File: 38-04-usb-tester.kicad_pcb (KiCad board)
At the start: 2 copper layers, 131.7 x 103.7 mm, 63 parts, among them J1 Conn_1x05, J2 USB_C_12401832E402A, J3 USB_C_12401832E402A, J4 USB_Micro-B_KH-MICRO5P-JN, J5 USB_Mini-B_U-M-M5DD-W-1, J6 USB3_A_HC-USB3.0-L168-WP, SW1 SW_SPDT, SW2 ZX-1.27BM-4PSMD, U1 STM32C031K6Tx

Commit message: pre commit to importing template
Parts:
- R1, R2, R3, R5: footprint Resistor_SMD:R_0201_0603Metric -> Resistor_SMD:R_0805_2012Metric_Pad1.20x1.40mm_HandSolder
- moved J1 54.7 mm to (183.9, 107.4), turned to 0 degrees
- moved C2 53.6 mm to (174.5, 123.2), turned to 0 degrees
- moved C1 40.9 mm to (131.2, 120.0), turned to -90 degrees
- moved C5 38.6 mm to (167.4, 120.4)
- moved SW2 36.6 mm to (172.3, 133.6)
- moved R5 29.8 mm to (171.2, 120.4)
- moved BT1 21.0 mm to (154.9, 114.2), turned to -90 degrees
- moved RN1 11.0 mm to (175.8, 101.3)
- moved RN2 11.0 mm to (175.8, 97.0)
- moved RN4 11.0 mm to (175.8, 87.6)
- moved RN5 11.0 mm to (175.8, 93.0)
- moved H10 10.1 mm to (118.5, 80.5)
- moved H2 9.78 mm to (191.3, 140.0)
- moved H5 8.98 mm to (118.5, 140.0)
- moved H7 8.18 mm to (196.9, 86.9)
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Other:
- board size 131.7 x 103.7 mm -> 125.9 x 97.8 mm

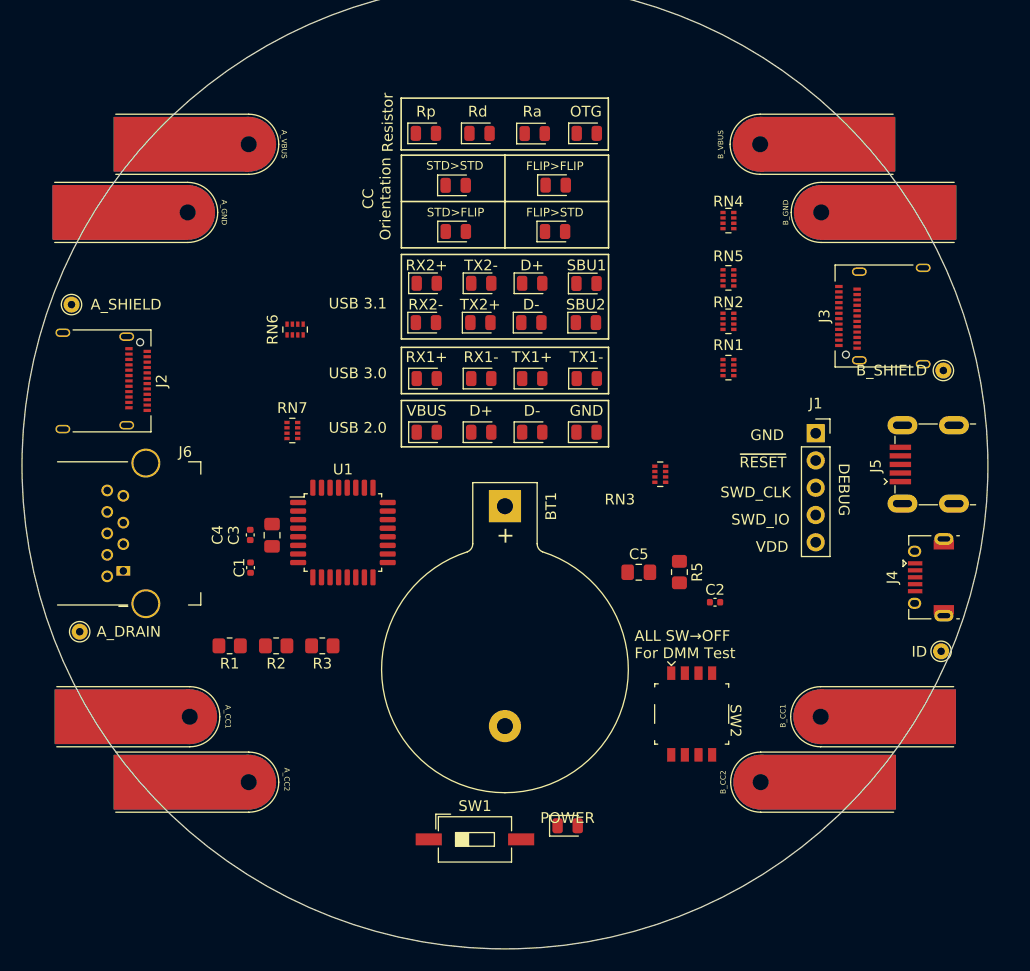
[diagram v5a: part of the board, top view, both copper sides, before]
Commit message: added defaults for jlpcb, fixed usb schematics
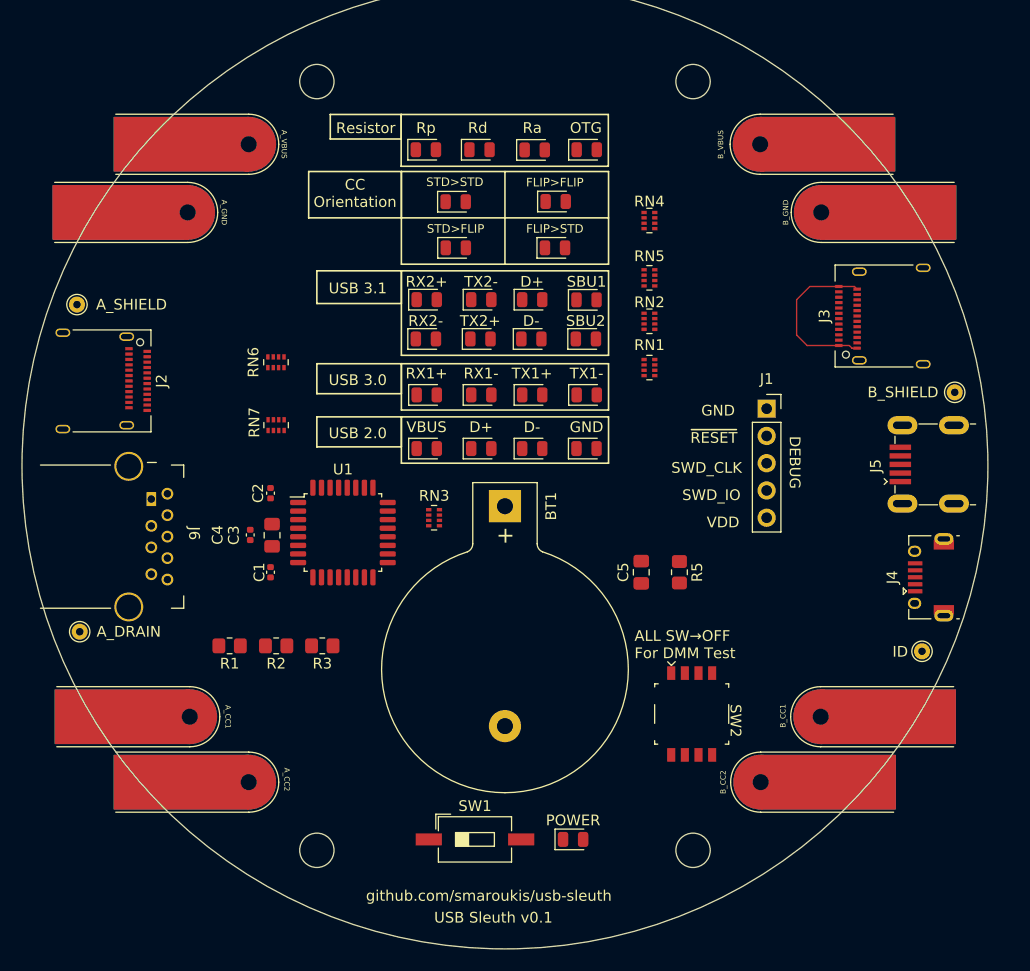
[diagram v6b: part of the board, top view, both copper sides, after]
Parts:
- added REF**: MountingHole_3.2mm_M3_DIN965, MountingHole:MountingHole_3.2mm_M3_DIN965, F.Cu at (137.4, 146.3)
- added REF**: MountingHole_3.2mm_M3_DIN965, MountingHole:MountingHole_3.2mm_M3_DIN965, F.Cu at (172.5, 146.3)
- added REF**: MountingHole_3.2mm_M3_DIN965, MountingHole:MountingHole_3.2mm_M3_DIN965, F.Cu at (137.4, 74.7)
- added REF**: MountingHole_3.2mm_M3_DIN965, MountingHole:MountingHole_3.2mm_M3_DIN965, F.Cu at (172.5, 74.7)
- moved C2 42.6 mm to (133.1, 113.0), turned to 90 degrees
- moved RN3 21.5 mm to (148.3, 115.3)
- moved RN1 7.36 mm to (168.4, 101.3)
- moved RN2 7.36 mm to (168.4, 97.0)
- moved RN4 7.36 mm to (168.4, 87.6)
- moved RN5 7.36 mm to (168.4, 93.0)
- moved J6 5.62 mm to (123.5, 117.1), turned to -90 degrees
- moved J1 5.11 mm to (179.3, 105.2)
- moved RN6 3.53 mm to (133.6, 100.8)
- moved H8 2.29 mm to (196.8, 103.6)
- moved C1 1.91 mm to (133.1, 120.4)
- moved H11 1.78 mm to (193.8, 127.8)
- moved RN7 1.59 mm to (133.6, 106.7), turned to -90 degrees
- moved D10 1.52 mm to (152.7, 103.9)
- moved D11 1.52 mm to (162.6, 103.9)
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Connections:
- H7 pad 1: /B_GND_B1 -> /B_GND_A1
- J3 pad A1: GND -> /B_GND_A1
- J3 pad A12: GND -> /B_GND_A1
- J3 pad B1: /B_GND_B1 -> /B_GND_A1
- J3 pad B12: GND -> /B_GND_A1
- SW2 pad 4: /B_GND_B1 -> /B_GND_A1
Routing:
- net /B_GND_A1: track 0.00 -> 16.4 mm
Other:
- board text added: "USB Sleuth v0.1"
- board text added: "github.com/smaroukis/usb-sleuth"

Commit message: started routing
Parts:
- moved R1 6.61 mm to (129.5, 120.7), turned to -90 degrees
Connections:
- H8 pad 1: /B_SHIELD -> /B_VBUS_A4
- J3 pad S1: /B_SHIELD -> /B_VBUS_A4
- J3 pad S2: /B_SHIELD -> /B_VBUS_A4
- J3 pad S3: /B_SHIELD -> /B_VBUS_A4
- J3 pad S4: /B_SHIELD -> /B_VBUS_A4
- J4 pad 5: GND -> /B_GND_A1
- J4 pad 6: /B_SHIELD -> /B_VBUS_A4
- J5 pad 5: GND -> /B_GND_A1
- J5 pad 6: /B_SHIELD -> /B_VBUS_A4
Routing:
- net /B_VBUS_A4: track 0.00 -> 125.6 mm, vias 0 -> 6
- net /B_CC1_SENS: track 0.00 -> 95.7 mm, vias 0 -> 2
- net /B_CC2_SENS: track 0.00 -> 95.5 mm, vias 0 -> 4
- net /B_GND_A1: track 16.4 -> 82.5 mm
- net /ID: track 0.00 -> 13.6 mm, vias 0 -> 2
- net /B_SSTx2-: track 0.00 -> 4.95 mm, vias 0 -> 1
- net /B_SSRx1+: track 0.00 -> 4.33 mm, vias 0 -> 1
- net /B_D2+: track 0.00 -> 3.68 mm, vias 0 -> 1
- net /B_SBU1: track 0.00 -> 2.86 mm
- net /B_SSRx1-: track 0.00 -> 2.82 mm, vias 0 -> 1
- net /B_SSTx2+: track 0.00 -> 2.54 mm, vias 0 -> 1
- net /B_SSRx2-: track 0.00 -> 2.20 mm
- net /B_D1+: track 0.00 -> 2.17 mm
- net /B_SSRx2+: track 0.00 -> 2.09 mm
- net /B_SSRTx1+: track 0.00 -> 1.52 mm
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- added copper zone on B.Cu, net GND

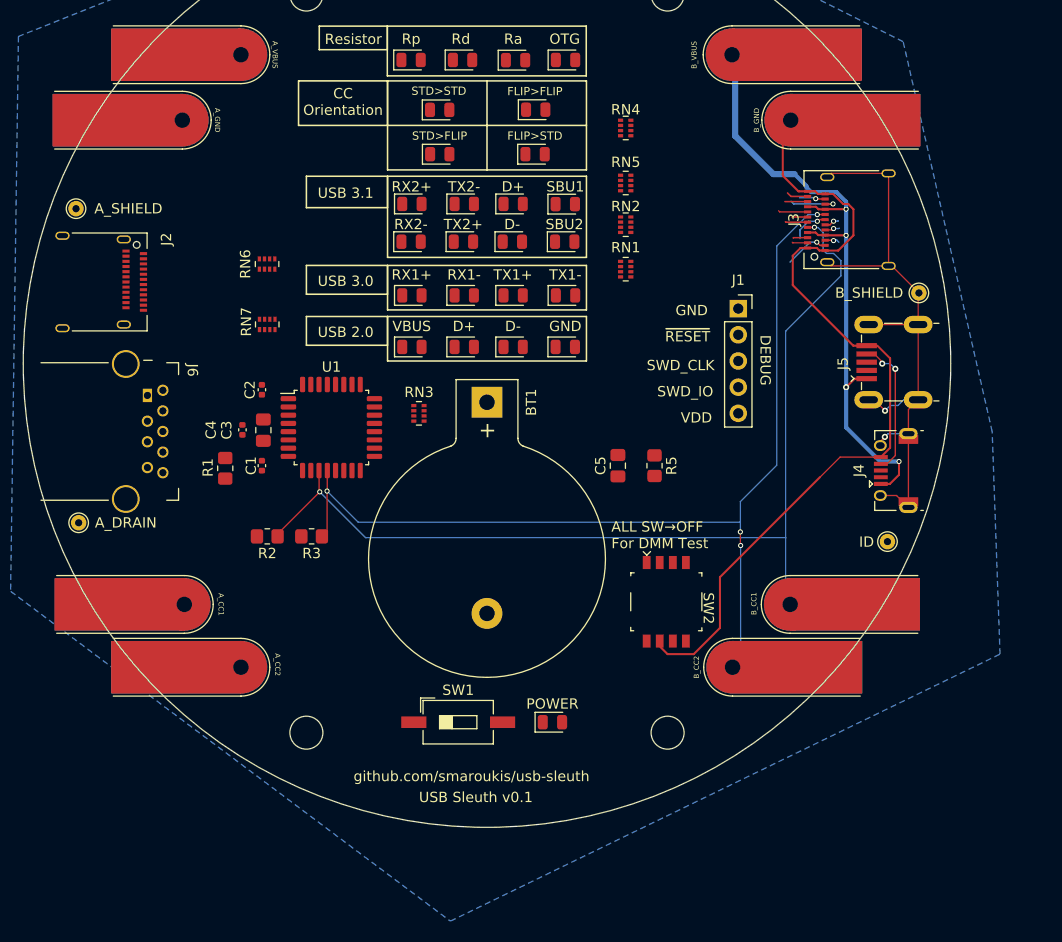
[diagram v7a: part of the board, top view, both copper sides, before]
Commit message: layout of LHS usb
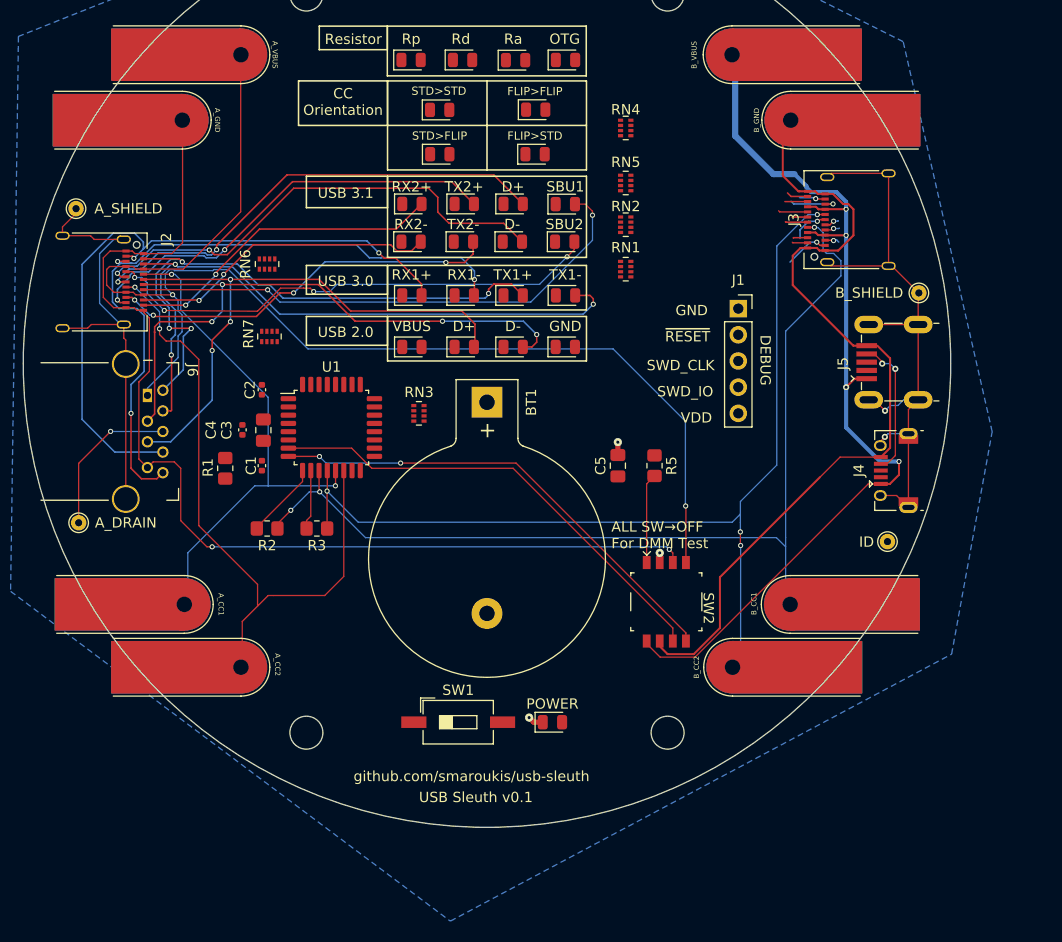
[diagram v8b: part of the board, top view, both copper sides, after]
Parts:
- moved D3 3.66 mm to (152.7, 98.7)
- moved D5 3.66 mm to (152.7, 95.0)
- moved RN7 1.19 mm to (133.8, 107.9)
- moved R3 0.92 mm to (138.4, 126.5)
- moved R2 0.76 mm to (133.6, 126.5)
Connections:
- H8 pad 1: /B_VBUS_A4 -> /B_SHIELD
- J3 pad S1: /B_VBUS_A4 -> /B_SHIELD
- J3 pad S2: /B_VBUS_A4 -> /B_SHIELD
- J3 pad S3: /B_VBUS_A4 -> /B_SHIELD
- J3 pad S4: /B_VBUS_A4 -> /B_SHIELD
- J4 pad 6: /B_VBUS_A4 -> /B_SHIELD
- J5 pad 6: /B_VBUS_A4 -> /B_SHIELD
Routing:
- net /A_VBUS: track 0.00 -> 123.1 mm, vias 0 -> 2
- net /A_GND: track 0.00 -> 103.2 mm, vias 0 -> 2
- net /A_SSRx1-: track 0.00 -> 67.6 mm, vias 0 -> 3
- net /A_SSTx1-: track 0.00 -> 65.1 mm, vias 0 -> 3
- net /A_SSRx1+: track 0.00 -> 64.7 mm, vias 0 -> 2
- net /A_CC2: track 0.00 -> 63.6 mm, vias 0 -> 2
- net /B_SHIELD: track 0.00 -> 63.0 mm, vias 0 -> 2
- net /A_D1-: track 0.00 -> 61.7 mm, vias 0 -> 4
- net /A_SSTx1+: track 0.00 -> 58.0 mm, vias 0 -> 4
- net /A_D1+: track 0.00 -> 57.1 mm, vias 0 -> 3
- net /A_SBU1: track 0.00 -> 51.4 mm, vias 0 -> 2
- net /A_CC1: track 0.00 -> 50.5 mm, vias 0 -> 2
- net /A_SBU2: track 0.00 -> 49.4 mm, vias 0 -> 4
- net /A_D2-: track 0.00 -> 47.0 mm, vias 0 -> 2
- net /A_VBUS_SENS: track 0.00 -> 46.5 mm, vias 0 -> 2
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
